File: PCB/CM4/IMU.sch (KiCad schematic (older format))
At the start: 4 parts, among them U2 MPU6000

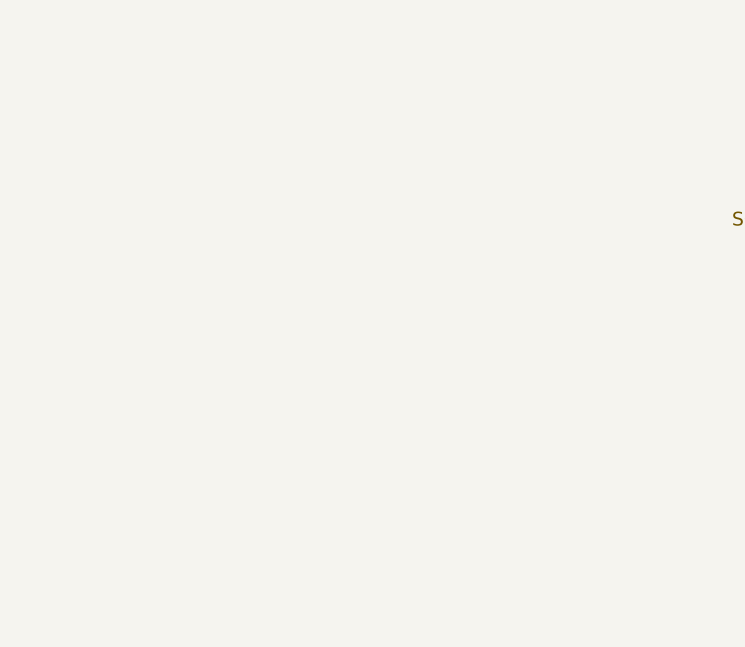
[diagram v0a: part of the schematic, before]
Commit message: Compass has been added
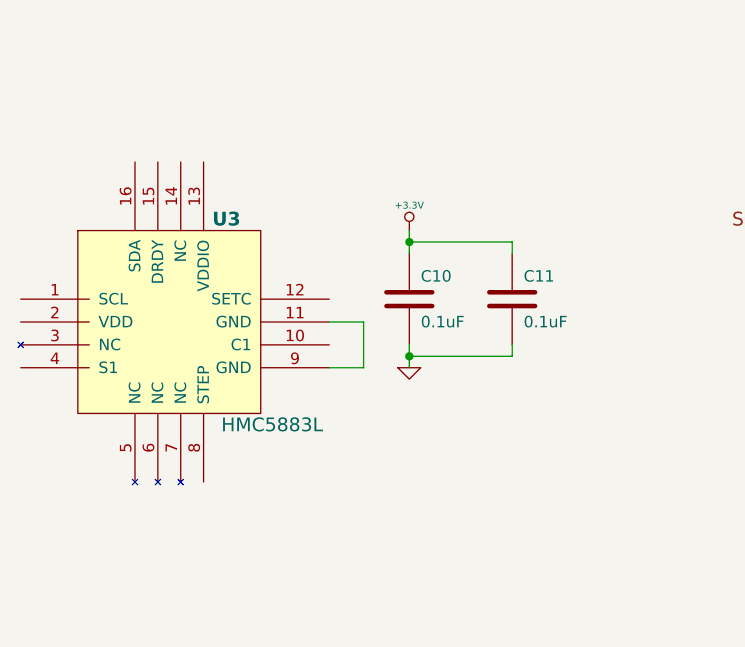
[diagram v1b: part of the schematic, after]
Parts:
- added C10, C11: 0.1uF, 0603, symbol C
- added U3: HMC5883L, QFN16P, symbol HMC5883L
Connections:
- net +3.3V: now also C10.1, C11.1
- net GND: now also C10.2, C11.2
- new net: U3.11 (GND), U3.9 (GND)
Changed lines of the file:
@@
-EESchema Schematic File Version 2  date Sat 03 Nov 2012 07:42:51 PM COT
+EESchema Schematic File Version 2  date Sat 03 Nov 2012 10:35:30 PM COT
 LIBS:power
 LIBS:device
@@
 LIBS:stm32f100vxx
 LIBS:mpu6000
+LIBS:hmc5883l
 LIBS:HackBo_DroneCore_CM4-cache
 EELAYER 25  0
@@
 $EndComp
 $Comp
-L +3.3V #PWR4
+L +3.3V #PWR6
 U 1 1 5095AC9D
 P 8250 3600
-F 0 "#PWR4" H 8250 3560 30  0001 C CNN
+F 0 "#PWR6" H 8250 3560 30  0001 C CNN
 F 1 "+3.3V" H 8250 3710 30  0000 C CNN
 	1    8250 3600
@@
 $EndComp
 $Comp
-L GND #PWR6
+L GND #PWR8
 U 1 1 5095ACAC
 P 8600 3700
-F 0 "#PWR6" H 8600 3700 30  0001 C CNN
+F 0 "#PWR8" H 8600 3700 30  0001 C CNN
 F 1 "GND" H 8600 3630 30  0001 C CNN
 	1    8600 3700
@@
 $EndComp
 $Comp
-L GND #PWR3
+L GND #PWR5
 U 1 1 5095ACB9
 P 8250 3250
-F 0 "#PWR3" H 8250 3250 30  0001 C CNN
+F 0 "#PWR5" H 8250 3250 30  0001 C CNN
 F 1 "GND" H 8250 3180 30  0001 C CNN
 	1    8250 3250
@@
 $EndComp
 $Comp
-L +3.3V #PWR5
+L +3.3V #PWR7
 U 1 1 5095ACEB
 P 8600 3100
-F 0 "#PWR5" H 8600 3060 30  0001 C CNN
+F 0 "#PWR7" H 8600 3060 30  0001 C CNN
 F 1 "+3.3V" H 8600 3210 30  0000 C CNN
 	1    8600 3100
@@
 	7400 1800 7400 1900
 $Comp
-L GND #PWR2
+L GND #PWR4
 U 1 1 5095AEE9
 P 7700 1900
-F 0 "#PWR2" H 7700 1900 30  0001 C CNN
+F 0 "#PWR4" H 7700 1900 30  0001 C CNN
 F 1 "GND" H 7700 1830 30  0001 C CNN
 	1    7700 1900
@@
 $EndComp
 $Comp
-L GND #PWR1
+L GND #PWR3
 U 1 1 5095AFB5
 P 7300 4900
-F 0 "#PWR1" H 7300 4900 30  0001 C CNN
+F 0 "#PWR3" H 7300 4900 30  0001 C CNN
 F 1 "GND" H 7300 4830 30  0001 C CNN
 	1    7300 4900
@@
 Wire Wire Line
 	7000 2400 6800 2400
+$Comp
+L HMC5883L U3
+U 1 1 5095E27D
+P 3350 3600
+F 0 "U3" H 3600 4100 60  0000 C CNB
+F 1 "HMC5883L" H 3800 3200 60  0000 C CNN
+F 2 "QFN16P" H 3350 3600 60  0001 C CNN
+	1    3350 3600
+	1    0    0    -1
+$EndComp
+$Comp
+L GND #PWR2
+U 1 1 5095E346
+P 4400 3750
+F 0 "#PWR2" H 4400 3750 30  0001 C CNN
+F 1 "GND" H 4400 3680 30  0001 C CNN
+	1    4400 3750
+	1    0    0    -1
+$EndComp
+$Comp
+L C C10
+U 1 1 5095E34C
+P 4400 3450
+F 0 "C10" H 4450 3550 50  0000 L CNN
+F 1 "0.1uF" H 4450 3350 50  0000 L CNN
+F 2 "0603" H 4400 3450 60  0001 C CNN
+	1    4400 3450
+	1    0    0    -1
+$EndComp
+$Comp
+L +3.3V #PWR1
+U 1 1 5095E352
+P 4400 3150
+F 0 "#PWR1" H 4400 3110 30  0001 C CNN
+F 1 "+3.3V" H 4400 3260 30  0000 C CNN
+	1    4400 3150
+	1    0    0    -1
+$EndComp
+Wire Wire Line
+	4400 3150 4400 3250
+Wire Wire Line
+	4400 3650 4400 3750
+$Comp
+L C C11
+U 1 1 5095E35A
+P 4850 3450
+F 0 "C11" H 4900 3550 50  0000 L CNN
+F 1 "0.1uF" H 4900 3350 50  0000 L CNN
+F 2 "0603" H 4850 3450 60  0001 C CNN
+	1    4850 3450
+	1    0    0    -1
+$EndComp
+Wire Wire Line
+	4850 3250 4850 3200
+Wire Wire Line
+	4850 3200 4400 3200
+Connection ~ 4400 3200
+Wire Wire Line
+	4400 3700 4850 3700
+Wire Wire Line
+	4850 3700 4850 3650
+Connection ~ 4400 3700
+Wire Wire Line
+	4050 3550 4200 3550
+Wire Wire Line
+	4200 3550 4200 3750
+Wire Wire Line
+	4200 3750 4050 3750
 $EndSCHEMATC

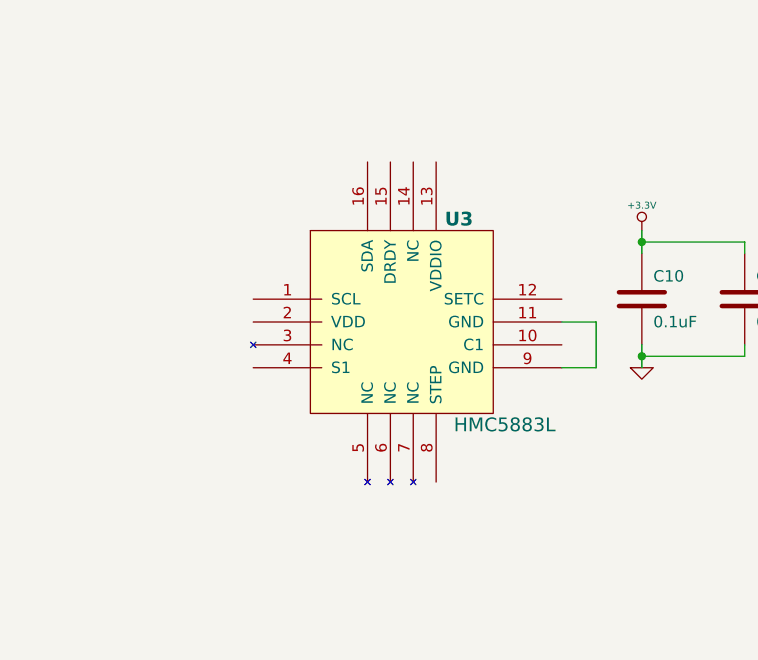
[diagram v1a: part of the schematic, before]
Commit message: Compass connected
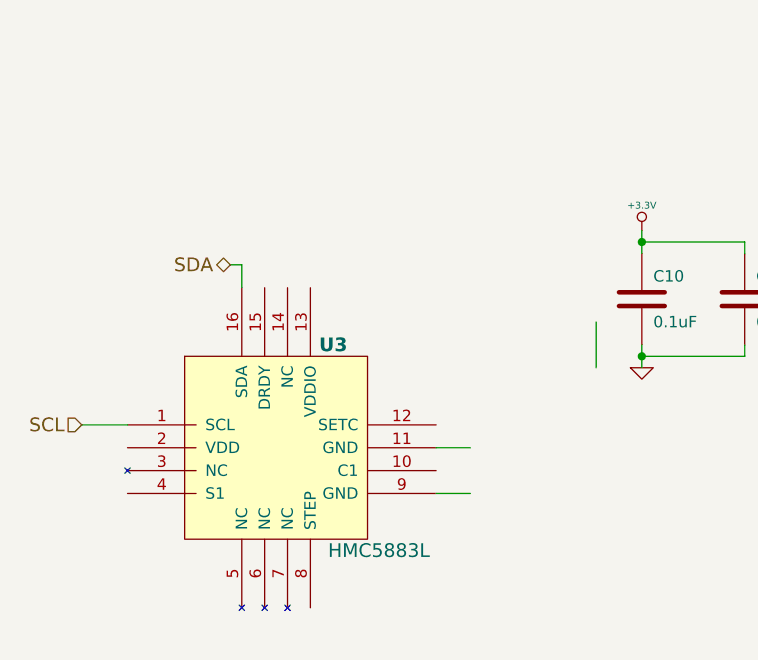
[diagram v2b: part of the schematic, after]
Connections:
- net labels added: SCL, SDA
- wire segments 25 -> 28
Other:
- moved on the sheet: U3
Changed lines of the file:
@@
-EESchema Schematic File Version 2  date Sat 03 Nov 2012 10:35:30 PM COT
+EESchema Schematic File Version 2  date Sat 03 Nov 2012 10:53:34 PM COT
 LIBS:power
 LIBS:device
@@
 $EndComp
 $Comp
-L +3.3V #PWR6
+L +3.3V #PWR01
 U 1 1 5095AC9D
 P 8250 3600
-F 0 "#PWR6" H 8250 3560 30  0001 C CNN
+F 0 "#PWR01" H 8250 3560 30  0001 C CNN
 F 1 "+3.3V" H 8250 3710 30  0000 C CNN
 	1    8250 3600
@@
 $EndComp
 $Comp
-L GND #PWR8
+L GND #PWR02
 U 1 1 5095ACAC
 P 8600 3700
-F 0 "#PWR8" H 8600 3700 30  0001 C CNN
+F 0 "#PWR02" H 8600 3700 30  0001 C CNN
 F 1 "GND" H 8600 3630 30  0001 C CNN
 	1    8600 3700
@@
 $EndComp
 $Comp
-L GND #PWR5
+L GND #PWR03
 U 1 1 5095ACB9
 P 8250 3250
-F 0 "#PWR5" H 8250 3250 30  0001 C CNN
+F 0 "#PWR03" H 8250 3250 30  0001 C CNN
 F 1 "GND" H 8250 3180 30  0001 C CNN
 	1    8250 3250
@@
 $EndComp
 $Comp
-L +3.3V #PWR7
+L +3.3V #PWR04
 U 1 1 5095ACEB
 P 8600 3100
-F 0 "#PWR7" H 8600 3060 30  0001 C CNN
+F 0 "#PWR04" H 8600 3060 30  0001 C CNN
 F 1 "+3.3V" H 8600 3210 30  0000 C CNN
 	1    8600 3100
@@
 	7400 1800 7400 1900
 $Comp
-L GND #PWR4
+L GND #PWR05
 U 1 1 5095AEE9
 P 7700 1900
-F 0 "#PWR4" H 7700 1900 30  0001 C CNN
+F 0 "#PWR05" H 7700 1900 30  0001 C CNN
 F 1 "GND" H 7700 1830 30  0001 C CNN
 	1    7700 1900
@@
 $EndComp
 $Comp
-L GND #PWR3
+L GND #PWR06
 U 1 1 5095AFB5
 P 7300 4900
-F 0 "#PWR3" H 7300 4900 30  0001 C CNN
+F 0 "#PWR06" H 7300 4900 30  0001 C CNN
 F 1 "GND" H 7300 4830 30  0001 C CNN
 	1    7300 4900
@@
 L HMC5883L U3
 U 1 1 5095E27D
-P 3350 3600
-F 0 "U3" H 3600 4100 60  0000 C CNB
-F 1 "HMC5883L" H 3800 3200 60  0000 C CNN
-F 2 "QFN16P" H 3350 3600 60  0001 C CNN
-	1    3350 3600
-	1    0    0    -1
-$EndComp
-$Comp
-L GND #PWR2
+P 2800 4150
+F 0 "U3" H 3050 4650 60  0000 C CNB
+F 1 "HMC5883L" H 3250 3750 60  0000 C CNN
+F 2 "QFN16P" H 2800 4150 60  0001 C CNN
+	1    2800 4150
+	1    0    0    -1
+$EndComp
+$Comp
+L GND #PWR07
 U 1 1 5095E346
 P 4400 3750
-F 0 "#PWR2" H 4400 3750 30  0001 C CNN
+F 0 "#PWR07" H 4400 3750 30  0001 C CNN
 F 1 "GND" H 4400 3680 30  0001 C CNN
 	1    4400 3750
@@
 $EndComp
 $Comp
-L +3.3V #PWR1
+L +3.3V #PWR08
 U 1 1 5095E352
 P 4400 3150
-F 0 "#PWR1" H 4400 3110 30  0001 C CNN
+F 0 "#PWR08" H 4400 3110 30  0001 C CNN
 F 1 "+3.3V" H 4400 3260 30  0000 C CNN
 	1    4400 3150
@@
 Connection ~ 4400 3700
 Wire Wire Line
-	4050 3550 4200 3550
+	3500 4100 3650 4100
 Wire Wire Line
 	4200 3550 4200 3750
 Wire Wire Line
-	4200 3750 4050 3750
+	3650 4300 3500 4300
+Text HLabel 2600 3300 0    60   BiDi ~ 0
+SDA
+Wire Wire Line
+	2600 3300 2650 3300
+Wire Wire Line
+	2650 3300 2650 3400
+Wire Wire Line
+	2150 4000 1950 4000
+Text HLabel 1950 4000 0    60   Input ~ 0
+SCL
 $EndSCHEMATC

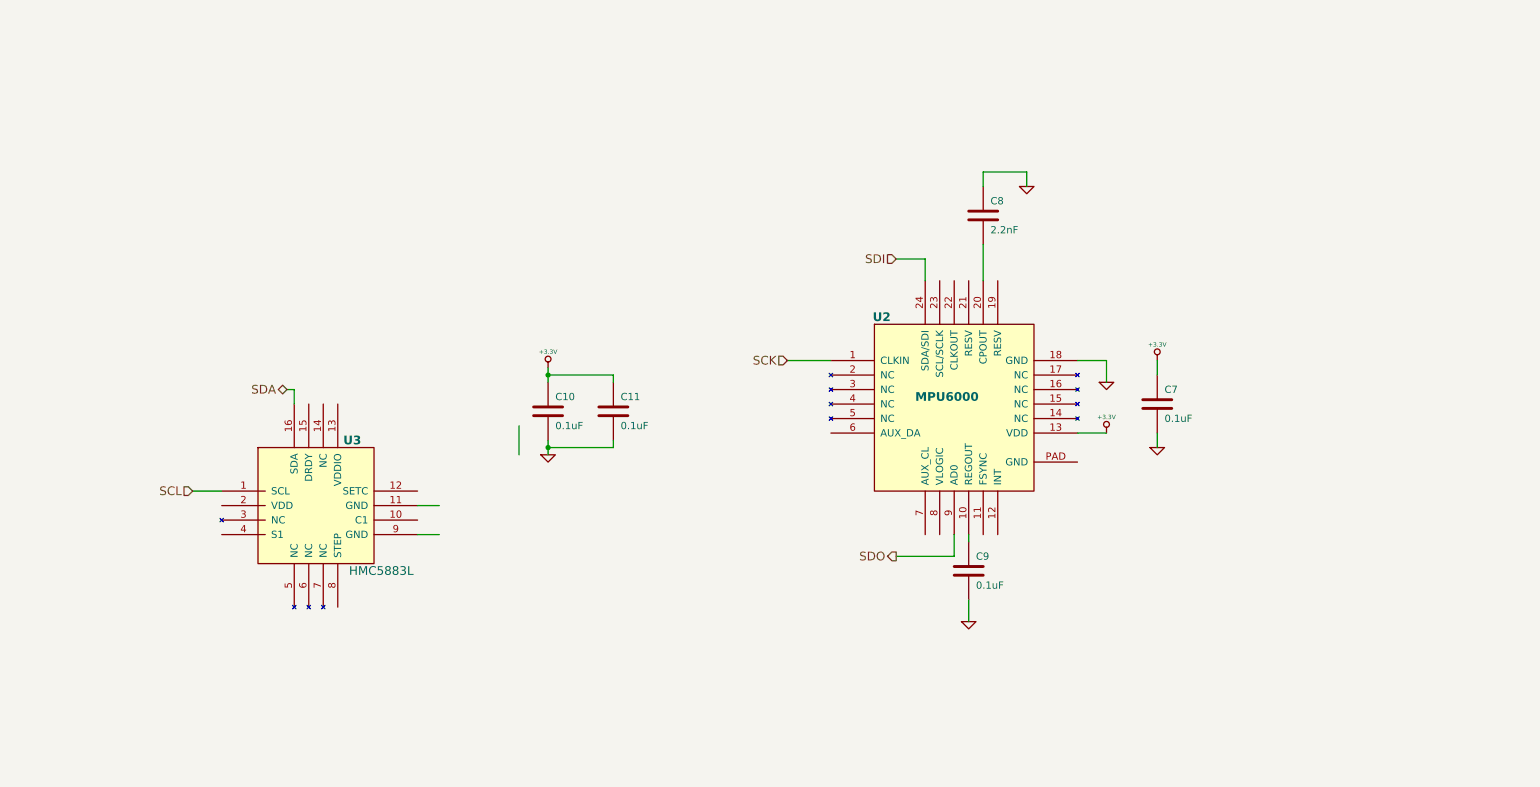
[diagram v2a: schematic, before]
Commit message: BMP085  altimeter has been added
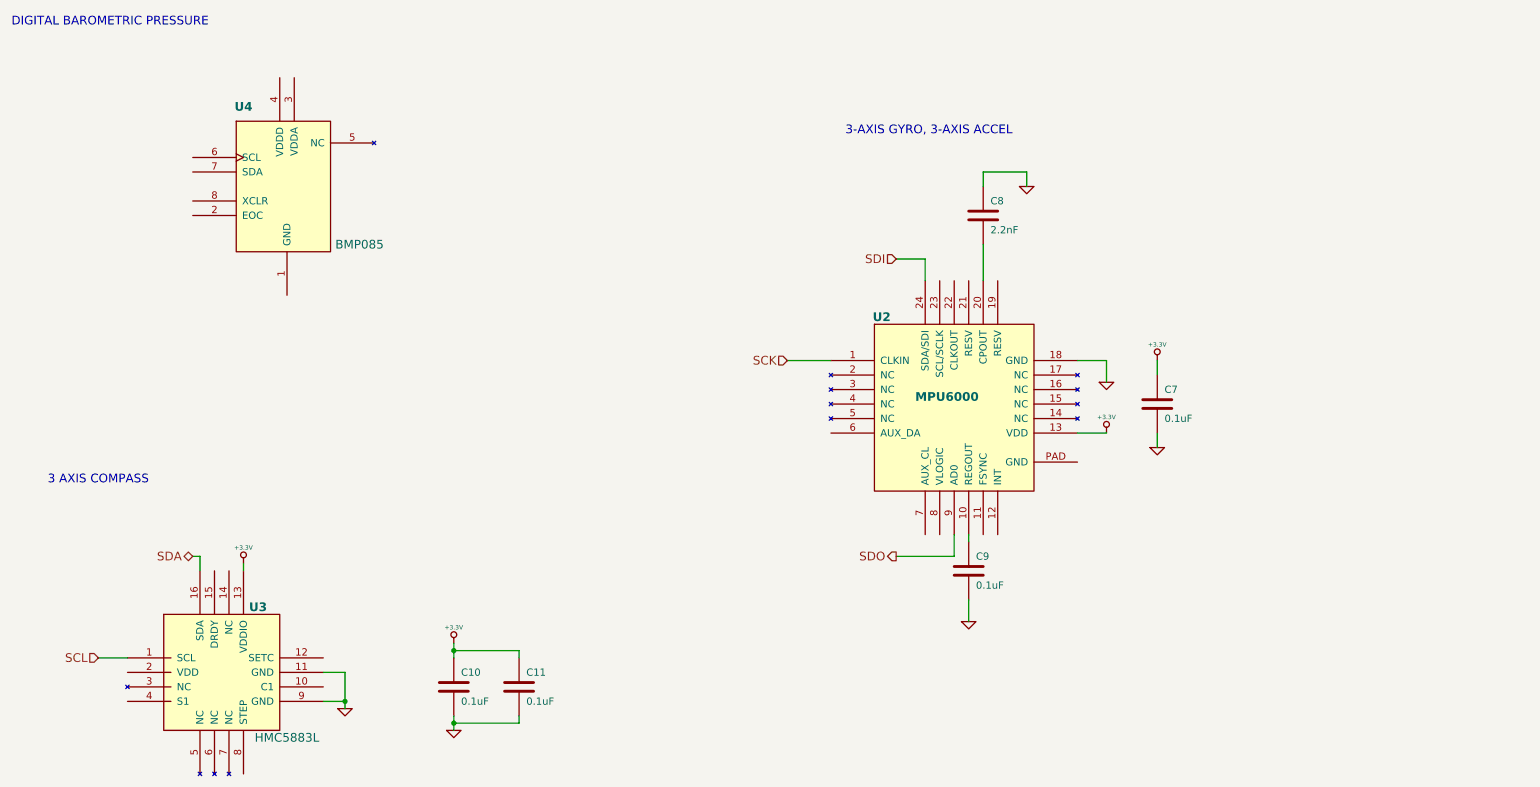
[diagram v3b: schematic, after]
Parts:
- added U4: BMP085, LCC8, symbol BMP085
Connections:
- wire segments 28 -> 29
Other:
- note added: "3 AXIS COMPASS\n\n\n"
- note added: "3-AXIS GYRO, 3-AXIS ACCEL"
- note added: "DIGITAL BAROMETRIC PRESSURE"
- moved on the sheet: C10, C11, U3
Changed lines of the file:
@@
-EESchema Schematic File Version 2  date Sat 03 Nov 2012 10:53:34 PM COT
+EESchema Schematic File Version 2  date Sun 04 Nov 2012 06:51:49 PM COT
 LIBS:power
 LIBS:device
@@
 LIBS:mpu6000
 LIBS:hmc5883l
+LIBS:bmp085
 LIBS:HackBo_DroneCore_CM4-cache
 EELAYER 25  0
@@
 L HMC5883L U3
 U 1 1 5095E27D
-P 2800 4150
-F 0 "U3" H 3050 4650 60  0000 C CNB
-F 1 "HMC5883L" H 3250 3750 60  0000 C CNN
-F 2 "QFN16P" H 2800 4150 60  0001 C CNN
-	1    2800 4150
+P 2150 5300
+F 0 "U3" H 2400 5800 60  0000 C CNB
+F 1 "HMC5883L" H 2600 4900 60  0000 C CNN
+F 2 "QFN16P" H 2150 5300 60  0001 C CNN
+	1    2150 5300
 	1    0    0    -1
 $EndComp
@@
 L GND #PWR07
 U 1 1 5095E346
-P 4400 3750
-F 0 "#PWR07" H 4400 3750 30  0001 C CNN
-F 1 "GND" H 4400 3680 30  0001 C CNN
-	1    4400 3750
+P 3750 5650
+F 0 "#PWR07" H 3750 5650 30  0001 C CNN
+F 1 "GND" H 3750 5580 30  0001 C CNN
+	1    3750 5650
 	1    0    0    -1
 $EndComp
@@
 L C C10
 U 1 1 5095E34C
-P 4400 3450
-F 0 "C10" H 4450 3550 50  0000 L CNN
-F 1 "0.1uF" H 4450 3350 50  0000 L CNN
-F 2 "0603" H 4400 3450 60  0001 C CNN
-	1    4400 3450
+P 3750 5350
+F 0 "C10" H 3800 5450 50  0000 L CNN
+F 1 "0.1uF" H 3800 5250 50  0000 L CNN
+F 2 "0603" H 3750 5350 60  0001 C CNN
+	1    3750 5350
 	1    0    0    -1
 $EndComp
@@
 L +3.3V #PWR08
 U 1 1 5095E352
-P 4400 3150
-F 0 "#PWR08" H 4400 3110 30  0001 C CNN
-F 1 "+3.3V" H 4400 3260 30  0000 C CNN
-	1    4400 3150
-	1    0    0    -1
-$EndComp
-Wire Wire Line
-	4400 3150 4400 3250
-Wire Wire Line
-	4400 3650 4400 3750
+P 3750 5050
+F 0 "#PWR08" H 3750 5010 30  0001 C CNN
+F 1 "+3.3V" H 3750 5160 30  0000 C CNN
+	1    3750 5050
+	1    0    0    -1
+$EndComp
+Wire Wire Line
+	3750 5050 3750 5150
+Wire Wire Line
+	3750 5550 3750 5650
 $Comp
 L C C11
 U 1 1 5095E35A
-P 4850 3450
-F 0 "C11" H 4900 3550 50  0000 L CNN
-F 1 "0.1uF" H 4900 3350 50  0000 L CNN
-F 2 "0603" H 4850 3450 60  0001 C CNN
-	1    4850 3450
-	1    0    0    -1
-$EndComp
-Wire Wire Line
-	4850 3250 4850 3200
-Wire Wire Line
-	4850 3200 4400 3200
-Connection ~ 4400 3200
-Wire Wire Line
-	4400 3700 4850 3700
-Wire Wire Line
-	4850 3700 4850 3650
-Connection ~ 4400 3700
-Wire Wire Line
-	3500 4100 3650 4100
-Wire Wire Line
-	4200 3550 4200 3750
-Wire Wire Line
-	3650 4300 3500 4300
-Text HLabel 2600 3300 0    60   BiDi ~ 0
+P 4200 5350
+F 0 "C11" H 4250 5450 50  0000 L CNN
+F 1 "0.1uF" H 4250 5250 50  0000 L CNN
+F 2 "0603" H 4200 5350 60  0001 C CNN
+	1    4200 5350
+	1    0    0    -1
+$EndComp
+Wire Wire Line
+	4200 5150 4200 5100
+Wire Wire Line
+	4200 5100 3750 5100
+Connection ~ 3750 5100
+Wire Wire Line
+	3750 5600 4200 5600
+Wire Wire Line
+	4200 5600 4200 5550
+Connection ~ 3750 5600
+Wire Wire Line
+	2850 5250 3000 5250
+Wire Wire Line
+	3000 5450 2850 5450
+Text HLabel 1950 4450 0    60   BiDi ~ 0
 SDA
 Wire Wire Line
-	2600 3300 2650 3300
-Wire Wire Line
-	2650 3300 2650 3400
-Wire Wire Line
-	2150 4000 1950 4000
-Text HLabel 1950 4000 0    60   Input ~ 0
+	1950 4450 2000 4450
+Wire Wire Line
+	2000 4450 2000 4550
+Wire Wire Line
+	1500 5150 1300 5150
+Text HLabel 1300 5150 0    60   Input ~ 0
 SCL
+$Comp
+L GND #PWR09
+U 1 1 5096F74E
+P 3000 5500
+F 0 "#PWR09" H 3000 5500 30  0001 C CNN
+F 1 "GND" H 3000 5430 30  0001 C CNN
+	1    3000 5500
+	1    0    0    -1
+$EndComp
+Wire Wire Line
+	3000 5250 3000 5500
+Connection ~ 3000 5450
+$Comp
+L +3.3V #PWR010
+U 1 1 5096F8D1
+P 2300 4500
+F 0 "#PWR010" H 2300 4460 30  0001 C CNN
+F 1 "+3.3V" H 2300 4610 30  0000 C CNN
+	1    2300 4500
+	1    0    0    -1
+$EndComp
+Wire Wire Line
+	2300 4500 2300 4550
+$Comp
+L BMP085 U4
+U 1 1 5096FBDC
+P 2600 1750
+F 0 "U4" H 2300 2150 60  0000 C CNB
+F 1 "BMP085" H 3100 1200 60  0000 C CNN
+F 2 "LCC8" H 2600 1750 60  0001 C CNN
+	1    2600 1750
+	1    0    0    -1
+$EndComp
+Text Notes 950  4150 0    60   ~ 0
+3 AXIS COMPASS\n\n\n
+Text Notes 700  800  0    60   ~ 0
+DIGITAL BAROMETRIC PRESSURE
+Text Notes 6450 1550 0    60   ~ 0
+3-AXIS GYRO, 3-AXIS ACCEL
 $EndSCHEMATC
